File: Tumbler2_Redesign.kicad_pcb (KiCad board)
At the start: 2 copper layers, 77 x 84 mm, 145 parts, among them J1 Conn_01x02, J2 Conn_01x05, J3 Conn_01x10, J4 Conn_01x10, J5 USB_C_Receptacle_USB2.0_16P, J6 USB_C_Receptacle_USB2.0_16P, J7 Conn_01x04, J8 Conn_01x06, J9 Conn_01x06, Q1 BC817, Q2 BC817, SW1 SW_Push, SW2 SW_Push, SW3 SW_Push, U1 AP63205WU, U10 MPU-6050, U11 TB6612FNG, U2 LM66100DCK, U3 AP63203WU, U4 ESP32-S3-WROOM-1, U5 CP2102N-A02-GQFN28R, U6 LM66100DCK, U7 LM66100DCK, U8 USBLC6-2SC6, U9 USBLC6-2SC6

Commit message: Delete footprints with no symbol
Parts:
- removed C17: 1uF, Capacitor_SMD:C_0603_1608Metric_Pad1.08x0.95mm_HandSolder
- removed C19, C22 (x2), C23 (x2), C24 (x2), C25 (x2), C3, C34, C6, C7, C8: 100nF, Capacitor_SMD:C_0603_1608Metric_Pad1.08x0.95mm_HandSolder
- removed C20: 10uF, Capacitor_SMD:C_0603_1608Metric_Pad1.08x0.95mm_HandSolder
- removed the C26 at (230.6, 121.9)
- removed C33: 10nF, Capacitor_SMD:C_0603_1608Metric_Pad1.08x0.95mm_HandSolder
- removed C35: 2.2nF, Capacitor_SMD:C_0603_1608Metric_Pad1.08x0.95mm_HandSolder
- removed C4: 22uF, Capacitor_SMD:C_0603_1608Metric_Pad1.08x0.95mm_HandSolder
- removed the D3 at (225.0, 113.3)
- removed the D4 at (225.0, 116.8)
- removed the D5 at (225.0, 120.4)
- removed the D6 at (225.0, 124.0)
- removed L1: 4.7uH, Tumbler2:VLS5045EX-4R7M
- removed Q2: BC817, Package_TO_SOT_SMD:SOT-23
- removed the R10 at (230.6, 111.8)
- removed R14, R16: 5k1, Resistor_SMD:R_0603_1608Metric_Pad0.98x0.95mm_HandSolder
- removed R3: 22k1, Resistor_SMD:R_0603_1608Metric_Pad0.98x0.95mm_HandSolder
- removed R4: 1k, Resistor_SMD:R_0603_1608Metric_Pad0.98x0.95mm_HandSolder
- removed R5: 47k5, Resistor_SMD:R_0603_1608Metric_Pad0.98x0.95mm_HandSolder
- removed TP3, TP8, TP9: TestPoint, TestPoint:TestPoint_Pad_D1.5mm
- removed U10: MPU-6050, Sensor_Motion:InvenSense_QFN-24_4x4mm_P0.5mm
- removed U5: CP2102N-A02-GQFN28R, Package_DFN_QFN:QFN-28-1EP_5x5mm_P0.5mm_EP3.35x3.35mm
- removed U6, U7: LM66100DCK, Package_TO_SOT_SMD:SOT-363_SC-70-6
- added D11: SS14, Diode_SMD:D_SMA, F.Cu at (177.7, 28.4)
- added D12: SS14, Diode_SMD:D_SMA, F.Cu at (177.7, 32.9)
- added D13: SS14, Diode_SMD:D_SMA, F.Cu at (189.6, 42.0)
- added D14: SS14, Diode_SMD:D_SMA, F.Cu at (189.6, 46.6)
- added Q3: MMBT3904, Package_TO_SOT_SMD:SOT-23, F.Cu at (196.4, 32.8)
- added R31: 5k1, Resistor_SMD:R_0603_1608Metric_Pad0.98x0.95mm_HandSolder, F.Cu at (195.8, 41.0)
- added R32: 5k1, Resistor_SMD:R_0603_1608Metric_Pad0.98x0.95mm_HandSolder, F.Cu at (195.8, 43.5)
- added U12: AMS1117-5.0, Package_TO_SOT_SMD:SOT-223-3_TabPin2, F.Cu at (178.6, 39.4)
- Q1: value BC817 -> MMBT3904
- U1: value AP63205WU -> CH340C; footprint Package_TO_SOT_SMD:TSOT-23-6 -> Package_SO:SOIC-16_3.9x9.9mm_P1.27mm
- U2: value LM66100DCK -> LSM6DSV; footprint Package_TO_SOT_SMD:SOT-363_SC-70-6 -> Package_LGA:LGA-14_3x2.5mm_P0.5mm_LayoutBorder3x4y
- moved Q1 121.5 mm to (196.4, 28.3)
- moved U2 57.4 mm to (176.3, 47.6), turned to 0 degrees
- moved U1 49.2 mm to (189.7, 32.0)
- moved C2 44.8 mm to (175.8, 50.8), turned to 0 degrees
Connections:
- C2 pad 1: VBAT -> 3.3V
- C5 pad 1: 5V_REG -> Net-(D11-A)
- TP2 pad 1: 5V_REG -> Net-(D11-A)
- U1 pad 1: 5V_REG -> GND
- U1 pad 2: VBAT -> /MCU/RXD
- U1 pad 3: VBAT -> /MCU/TXD
- U1 pad 4: GND -> 3.3V
- U1 pad 5: Net-(U1-SW) -> /MCU/DP
- U1 pad 6: Net-(U1-BST) -> /MCU/DM
- U2 pad 1: 5V_REG -> 3.3V
- U2 pad 3: 5V -> GND
- U2 pad 4: unconnected-(U2-NC-Pad4) -> /MCU/INT
- U2 pad 5: GND -> 3.3V
- U2 pad 6: 5V -> GND

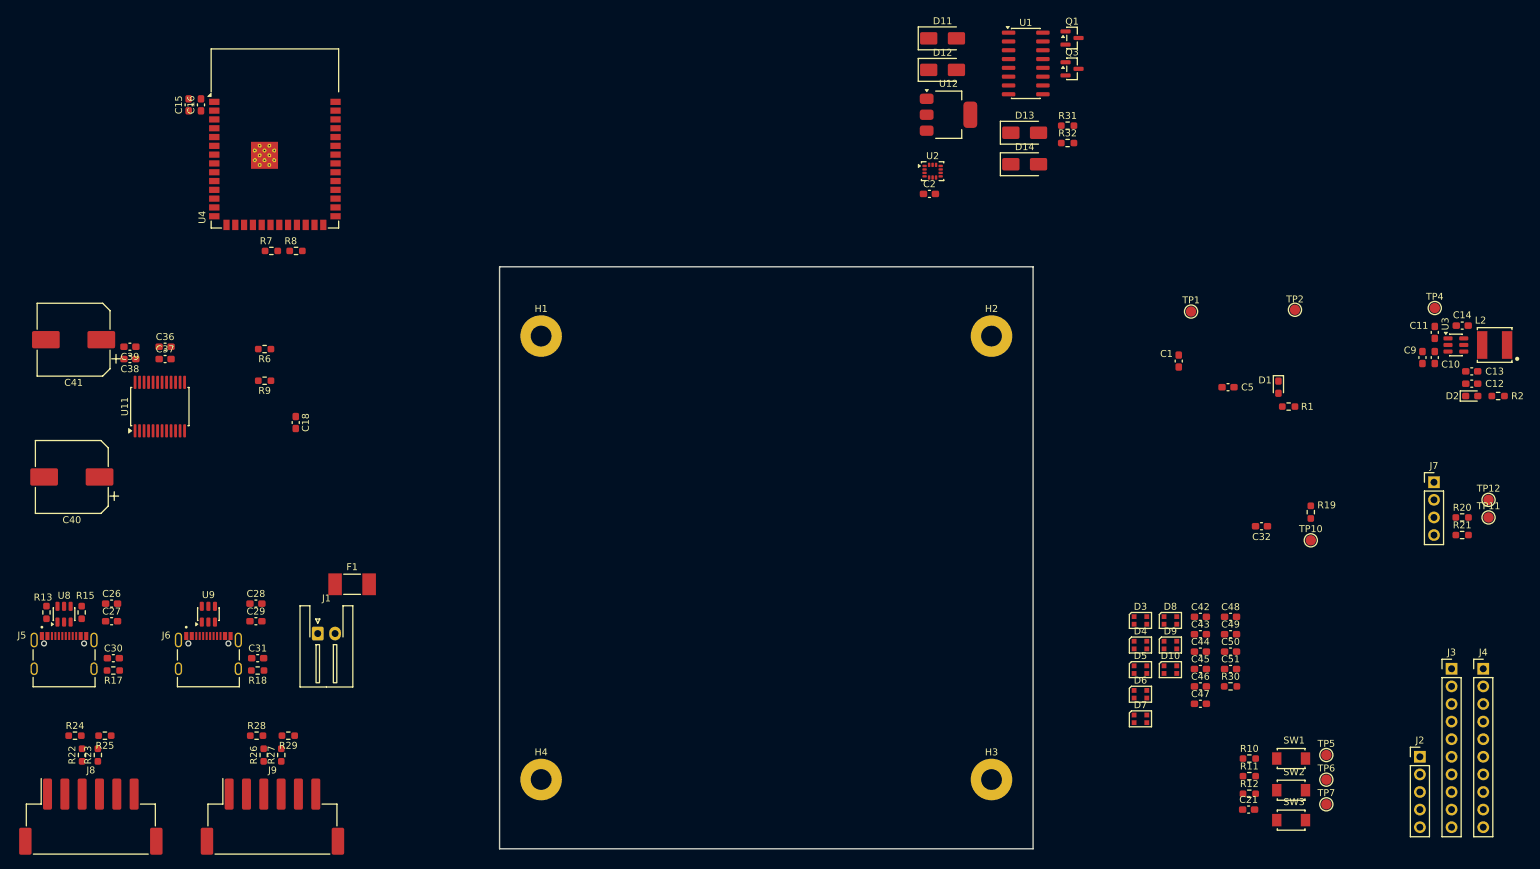
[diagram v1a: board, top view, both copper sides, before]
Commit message: Use basic parts where possible
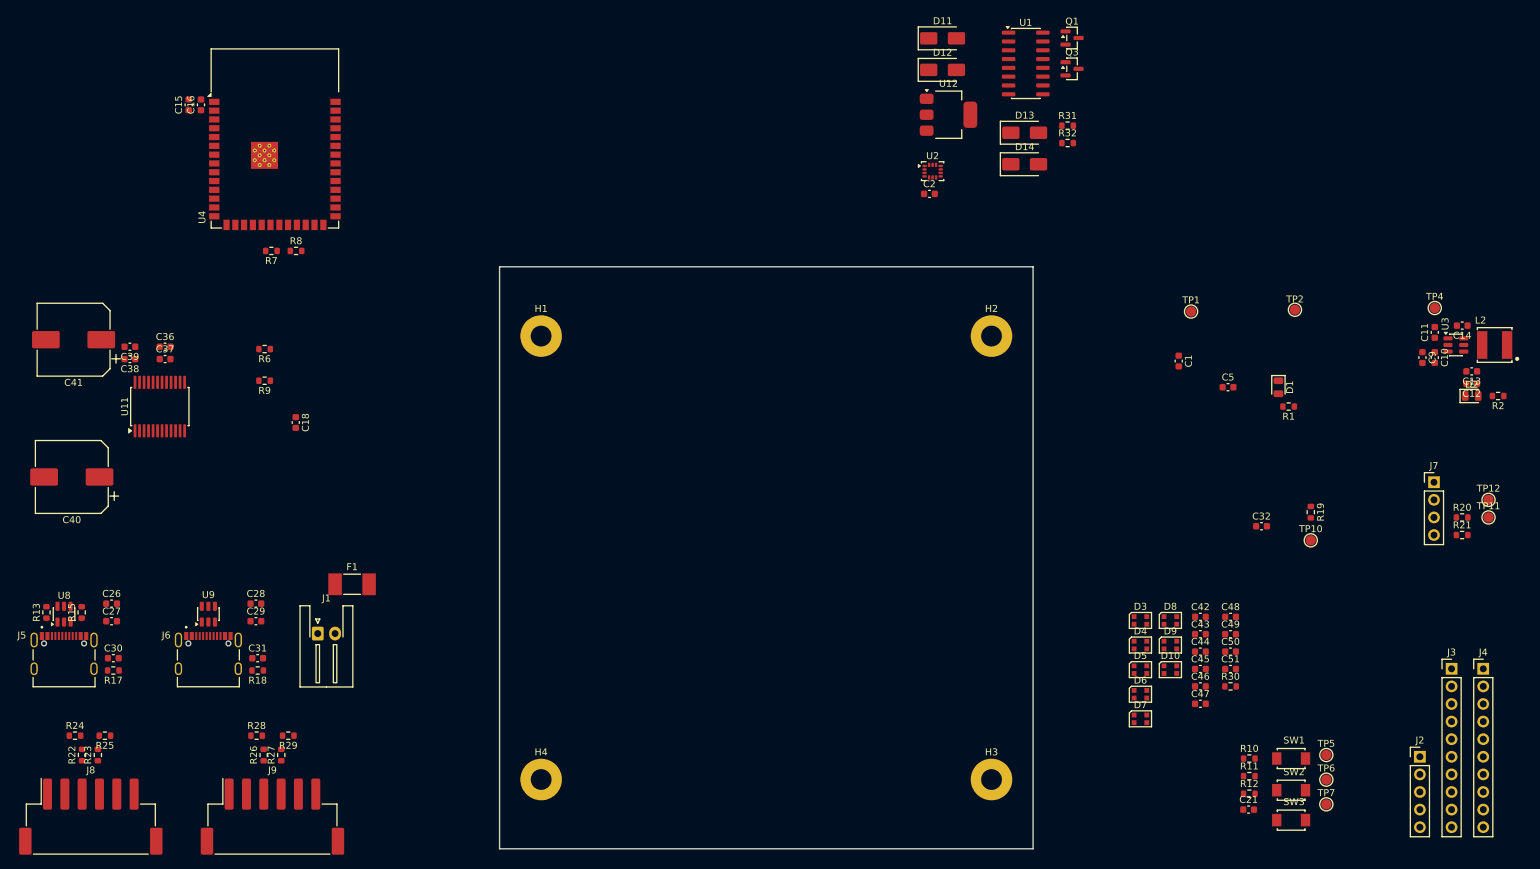
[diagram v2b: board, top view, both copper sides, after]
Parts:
- C1, C10, C11, C12, C13, C14, C15, C16, C18, C2, C21, C26, C27, C28, C29, C30, C31, C32, C36, C37, C38, C39, C42, C43, C44, C45, C46, C47, C48, C49, C5, C50, C51, C9: footprint Capacitor_SMD:C_0603_1608Metric_Pad1.08x0.95mm_HandSolder -> Capacitor_SMD:C_0603_1608Metric
- D1, D2: footprint LED_SMD:LED_0603_1608Metric_Pad1.05x0.95mm_HandSolder -> LED_SMD:LED_0805_2012Metric
- R1, R10, R11, R12, R13, R15, R17, R18, R19, R2, R20, R21, R22, R23, R24, R25, R26, R27, R28, R29, R30, R31, R32, R6, R7, R8, R9: footprint Resistor_SMD:R_0603_1608Metric_Pad0.98x0.95mm_HandSolder -> Resistor_SMD:R_0603_1608Metric

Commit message: Group components
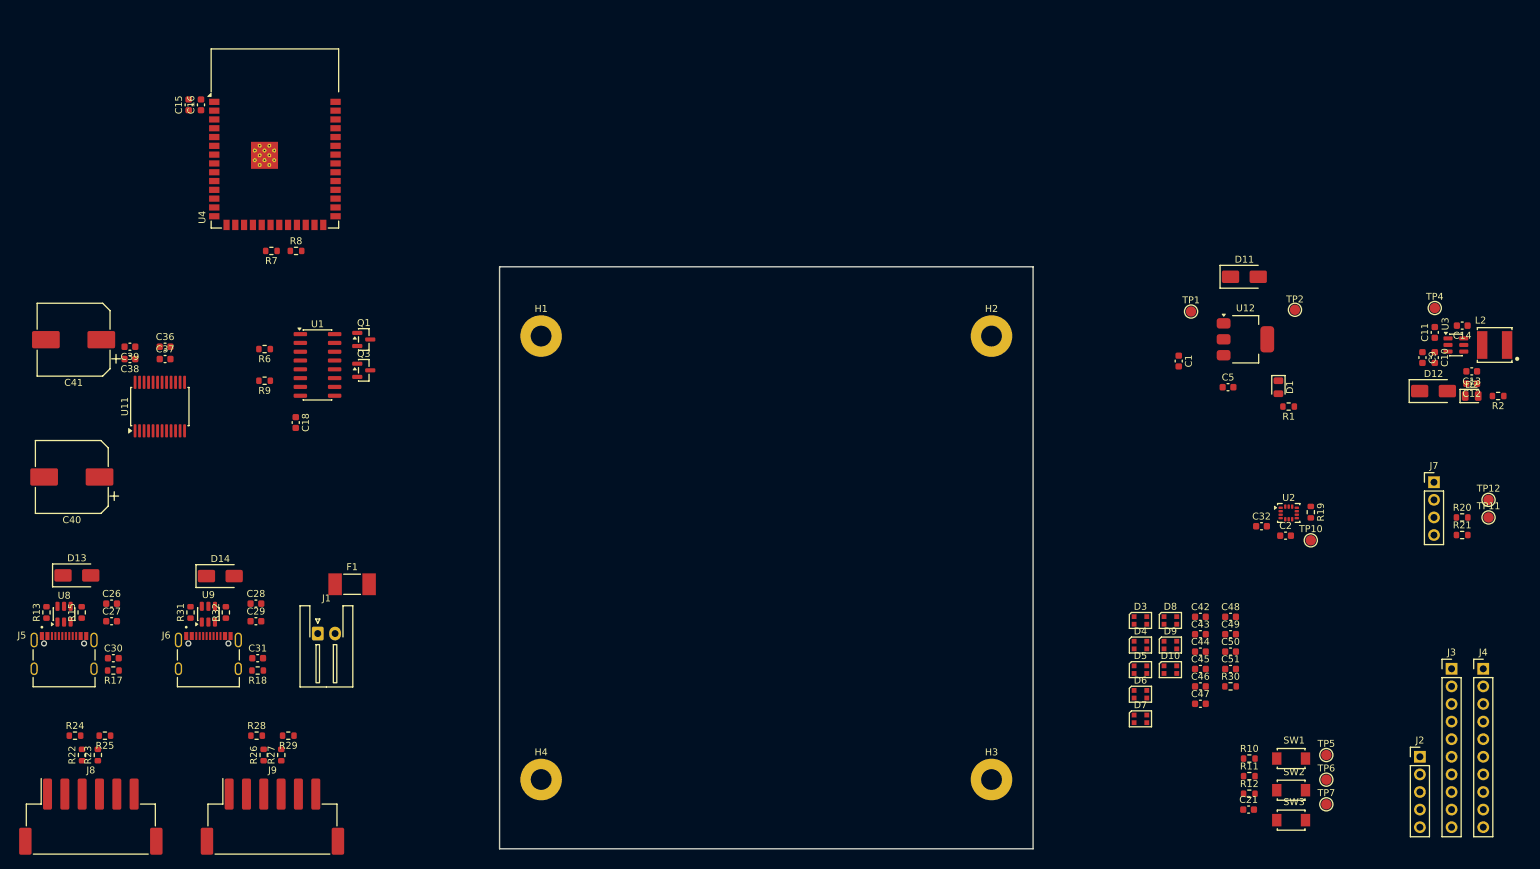
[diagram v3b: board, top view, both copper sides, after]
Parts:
- moved D13 151.0 mm to (52.8, 105.9)
- moved R31 144.8 mm to (69.2, 111.2), turned to 90 degrees
- moved R32 139.1 mm to (74.3, 111.2), turned to 90 degrees
- moved D14 130.4 mm to (73.5, 106.0)
- moved Q1 111.1 mm to (94.2, 71.8)
- moved Q3 111.1 mm to (94.2, 76.3)
- moved U1 111.1 mm to (87.5, 75.5)
- moved D12 84.7 mm to (248.6, 79.3)
- moved C2 71.2 mm to (227.2, 100.2)
- moved U2 71.2 mm to (227.7, 96.9)
- moved D11 55.5 mm to (221.3, 62.8)
- moved U12 53.7 mm to (221.5, 71.8)
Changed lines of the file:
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@@
 	(footprint "Resistor_SMD:R_0603_1608Metric"
 		(layer "F.Cu")
-		(at 195.7875 40.99)
+		(at 69.2 111.246 90)
 		(descr "Resistor SMD 0603 (1608 Metric), square (rectangular) end terminal, IPC-7351 nominal, (Body size source: IPC-SM-782 page 72, https://www.pcb-3d.com/wordpress/wp-content/uploads/ipc-sm-782a_amendment_1_and_2.pdf), generated with kicad-footprint-generator")
 		(tags "resistor")
 		(property "Reference" "R31"
-			(at 0 -1.43 0)
+			(at 0 -1.43 90)
 			(layer "F.SilkS")
 			(effects
@@
 		)
 		(property "Value" "5k1"
-			(at 0 1.43 0)
+			(at 0 1.43 90)
 			(layer "F.Fab")
 			(effects
@@
 		)
 		(property "Datasheet" "~"
-			(at 0 0 0)
+			(at 0 0 90)
 			(layer "F.Fab")
 			(hide yes)
@@
 		)
 		(property "Description" "Resistor"
-			(at 0 0 0)
+			(at 0 0 90)
 			(layer "F.Fab")
 			(hide yes)
@@
 		)
 		(property "LCSC PN" "C23186"
-			(at 0 0 0)
+			(at 0 0 90)
 			(unlocked yes)
 			(layer "F.Fab")
@@
 		)
 		(fp_text user "${REFERENCE}"
-			(at 0 0 0)
+			(at 0 0 90)
 			(layer "F.Fab")
 			(effects
@@
 		)
 		(pad "1" smd roundrect
-			(at -0.825 0)
+			(at -0.825 0 90)
 			(size 0.8 0.95)
 			(layers "F.Cu" "F.Mask" "F.Paste")
@@
 		)
 		(pad "2" smd roundrect
-			(at 0.825 0)
+			(at 0.825 0 90)
 			(size 0.8 0.95)
 			(layers "F.Cu" "F.Mask" "F.Paste")
@@
 	(footprint "Diode_SMD:D_SMA"
 		(layer "F.Cu")
-		(at 189.5925 46.56)
+		(at 73.5 106)
 		(descr "Diode SMA (DO-214AC)")
 		(tags "Diode SMA (DO-214AC)")
@@
 	(footprint "Package_TO_SOT_SMD:SOT-23"
 		(layer "F.Cu")
-		(at 196.4275 32.79)
+		(at 94.205 76.3)
 		(descr "SOT, 3 Pin (JEDEC TO-236 Var AB https://www.jedec.org/document_search?search_api_views_fulltext=TO-236), generated with kicad-footprint-generator ipc_gullwing_generator.py")
 		(tags "SOT TO_SOT_SMD")
@@
 	(footprint "Package_LGA:LGA-14_3x2.5mm_P0.5mm_LayoutBorder3x4y"
 		(layer "F.Cu")
-		(at 176.3025 47.56)
+		(at 227.7 96.8875)
 		(descr "LGA, 14 Pin (https://www.st.com/resource/en/datasheet/lsm6ds3tr-c.pdf), generated with kicad-footprint-generator ipc_noLead_generator.py")
 		(tags "LGA NoLead")
@@
 	(footprint "Package_TO_SOT_SMD:SOT-23"
 		(layer "F.Cu")
-		(at 196.4275 28.34)
+		(at 94.205 71.85)
 		(descr "SOT, 3 Pin (JEDEC TO-236 Var AB https://www.jedec.org/document_search?search_api_views_fulltext=TO-236), generated with kicad-footprint-generator ipc_gullwing_generator.py")
 		(tags "SOT TO_SOT_SMD")
@@
 	(footprint "Diode_SMD:D_SMA"
 		(layer "F.Cu")
-		(at 177.7425 28.39)
+		(at 221.3 62.8)
 		(descr "Diode SMA (DO-214AC)")
 		(tags "Diode SMA (DO-214AC)")
@@
 	(footprint "Resistor_SMD:R_0603_1608Metric"
 		(layer "F.Cu")
-		(at 195.7875 43.5)
+		(at 74.3 111.246 90)
 		(descr "Resistor SMD 0603 (1608 Metric), square (rectangular) end terminal, IPC-7351 nominal, (Body size source: IPC-SM-782 page 72, https://www.pcb-3d.com/wordpress/wp-content/uploads/ipc-sm-782a_amendment_1_and_2.pdf), generated with kicad-footprint-generator")
 		(tags "resistor")
 		(property "Reference" "R32"
-			(at 0 -1.43 0)
+			(at 0 -1.43 90)
 			(layer "F.SilkS")
 			(effects
@@
 		)
 		(property "Value" "5k1"
-			(at 0 1.43 0)
+			(at 0 1.43 90)
 			(layer "F.Fab")
 			(effects
@@
 		)
 		(property "Datasheet" "~"
-			(at 0 0 0)
+			(at 0 0 90)
 			(layer "F.Fab")
 			(hide yes)
@@
 		)
 		(property "Description" "Resistor"
-			(at 0 0 0)
+			(at 0 0 90)
 			(layer "F.Fab")
 			(hide yes)
@@
 		)
 		(property "LCSC PN" "C23186"
-			(at 0 0 0)
+			(at 0 0 90)
 			(unlocked yes)
 			(layer "F.Fab")
@@
 		)
 		(fp_text user "${REFERENCE}"
-			(at 0 0 0)
+			(at 0 0 90)
 			(layer "F.Fab")
 			(effects
@@
 		)
 		(pad "1" smd roundrect
-			(at -0.825 0)
+			(at -0.825 0 90)
 			(size 0.8 0.95)
 			(layers "F.Cu" "F.Mask" "F.Paste")
@@
 		)
 		(pad "2" smd roundrect
-			(at 0.825 0)
+			(at 0.825 0 90)
 			(size 0.8 0.95)
 			(layers "F.Cu" "F.Mask" "F.Paste")
@@
 	(footprint "Capacitor_SMD:C_0603_1608Metric"
 		(layer "F.Cu")
-		(at 175.8475 50.84)
+		(at 227.245 100.1675)
 		(descr "Capacitor SMD 0603 (1608 Metric), square (rectangular) end terminal, IPC-7351 nominal, (Body size source: IPC-SM-782 page 76, https://www.pcb-3d.com/wordpress/wp-content/uploads/ipc-sm-782a_amendment_1_and_2.pdf), generated with kicad-footprint-generator")
 		(tags "capacitor")
@@
 	(footprint "Package_SO:SOIC-16_3.9x9.9mm_P1.27mm"
 		(layer "F.Cu")
-		(at 189.7475 32.015)
+		(at 87.525 75.525)
 		(descr "SOIC, 16 Pin (JEDEC MS-012, variation AC, https://www.jedec.org/document_search?search_api_views_fulltext=MS-012, https://www.analog.com/media/en/package-pcb-resources/package/pkg_pdf/soic_narrow-r/r_16.pdf), generated with kicad-footprint-generator ipc_gullwing_generator.py")
 		(tags "SOIC SO 16-pin-NSOP R-16 R-16-S D0016A M2B SO16 SOT109-1 751B SOIC_N narrow")
@@
 	(footprint "Diode_SMD:D_SMA"
 		(layer "F.Cu")
-		(at 177.7425 32.94)
+		(at 248.6 79.3)
 		(descr "Diode SMA (DO-214AC)")
 		(tags "Diode SMA (DO-214AC)")
@@
 	(footprint "Diode_SMD:D_SMA"
 		(layer "F.Cu")
-		(at 189.5925 42.01)
+		(at 52.8 105.9)
 		(descr "Diode SMA (DO-214AC)")
 		(tags "Diode SMA (DO-214AC)")
@@
 	(footprint "Package_TO_SOT_SMD:SOT-223-3_TabPin2"
 		(layer "F.Cu")
-		(at 178.5975 39.415)
+		(at 221.455 71.825)
 		(descr "module CMS SOT223 4 pins")
 		(tags "CMS SOT")

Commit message: Sketch out component placement
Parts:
- removed C46: 10uF, Capacitor_SMD:C_0603_1608Metric
- H1, H2, H3, H4: footprint MountingHole:MountingHole_3mm_Pad -> MountingHole:MountingHole_3mm_Pad_Via
- moved J8 141.4 mm to (184.9, 85.3), turned to 90 degrees
- moved J2 134.6 mm to (129.8, 65.3), turned to 90 degrees
- moved R22 130.3 mm to (175.8, 86.6), turned to 180 degrees
- moved R23 129.0 mm to (175.8, 84.3), turned to 180 degrees
- moved R24 127.4 mm to (173.0, 87.6), turned to 90 degrees
- moved R25 124.8 mm to (173.0, 83.3), turned to -90 degrees
- moved TP7 115.0 mm to (124.0, 102.9), turned to -90 degrees
- moved C40 112.8 mm to (164.8, 91.2), turned to 0 degrees
- moved C41 112.7 mm to (164.8, 78.5), turned to 0 degrees
- moved SW3 112.6 mm to (124.0, 98.3), turned to -90 degrees
- moved TP6 108.6 mm to (129.5, 102.9), turned to -90 degrees
- moved D12 108.3 mm to (142.5, 100.8)
- moved L2 108.2 mm to (151.4, 94.2)
- moved C12 108.2 mm to (148.1, 99.8)
- moved C13 108.2 mm to (148.1, 98.0)
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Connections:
- net /MCU/INT renamed /MCU/INT1
